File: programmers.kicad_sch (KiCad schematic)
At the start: 9 parts, among them J10 Conn_ARM_JTAG_SWD_10, SW1 KMR231NG LFS, U8 MKL02Z32VFG4

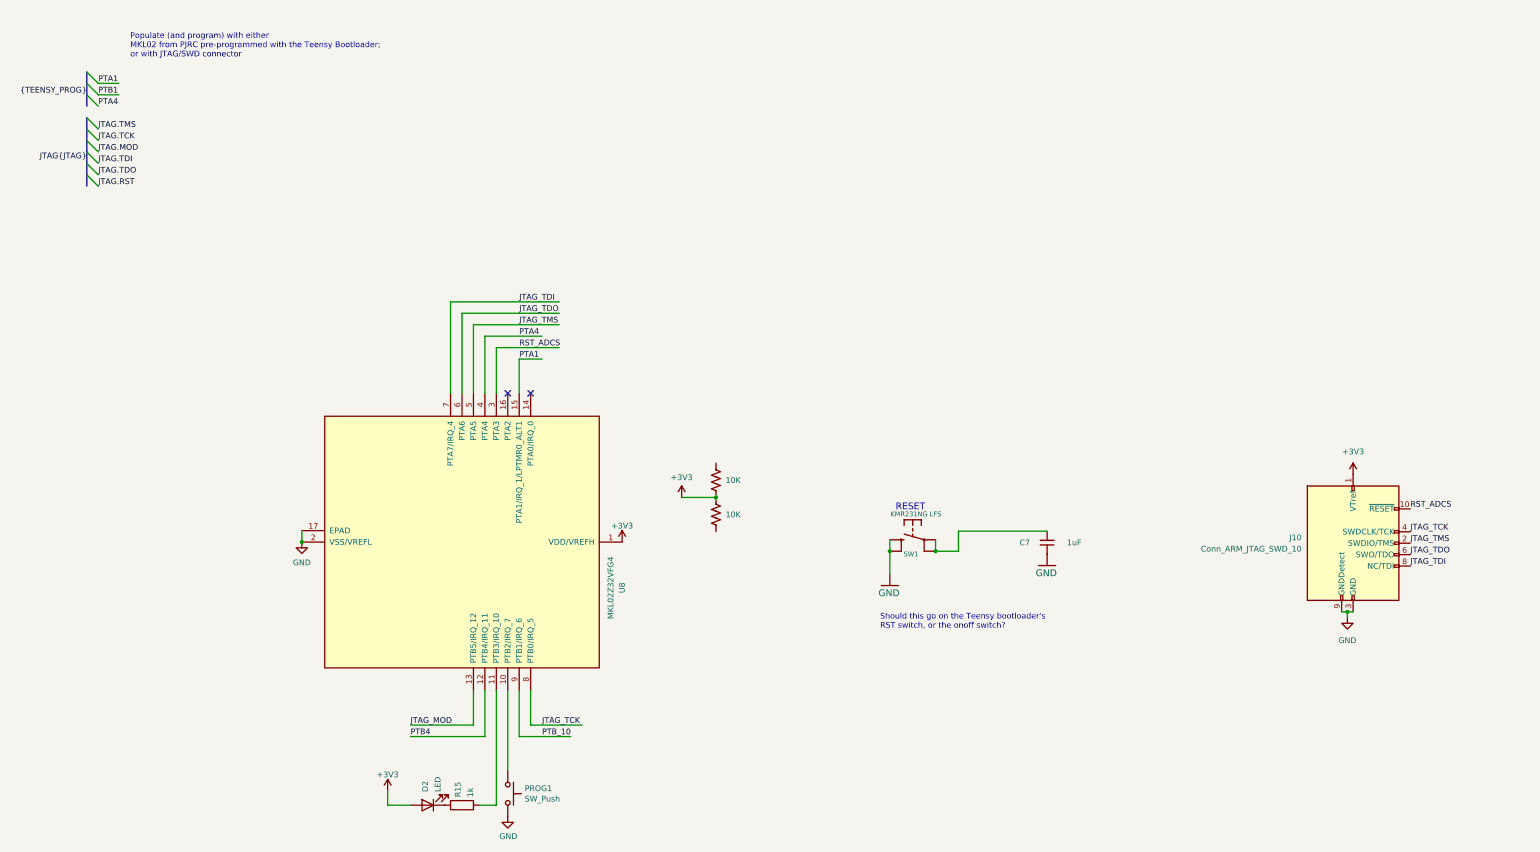
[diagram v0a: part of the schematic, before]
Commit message: schematic update
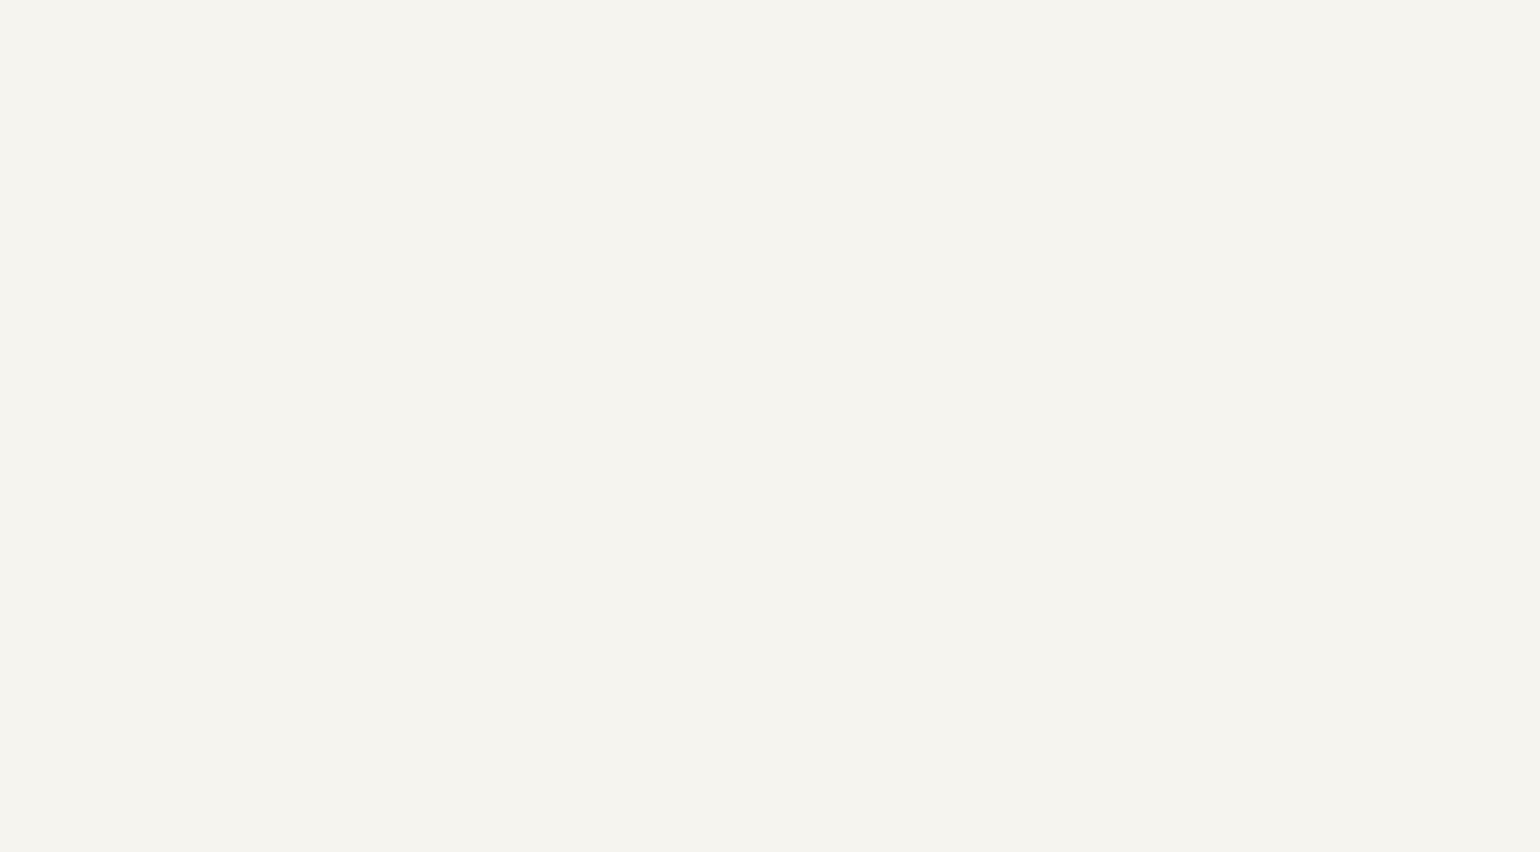
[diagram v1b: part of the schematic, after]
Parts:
- removed C7: 1uF, Capacitor_SMD:C_0603_1608Metric, symbol mainboard:C_Small
- removed D2: LED, LED_SMD:LED_0402_1005Metric, symbol Device:LED
- removed J10: Conn_ARM_JTAG_SWD_10, Connector_PinHeader_1.27mm:PinHeader_2x05_P1.27mm_Vertical_SMD, symbol Connector:Conn_ARM_JTAG_SWD_10
- removed PROG1: SW_Push, ToyTronics:KMR241GLFS, symbol Switch:SW_Push
- removed R15: 1k, Resistor_SMD:R_0402_1005Metric, symbol Device:R
- removed R17, R20: 10K, Resistor_SMD:R_0603_1608Metric, symbol Device:R_US
- removed SW1: KMR231NG LFS, mainboard:BTN_KMR2_4.6X2.8, symbol mainboard:SWITCH_SMT4.6X2.8
- removed U8: MKL02Z32VFG4, Package_DFN_QFN:QFN-16-1EP_3x3mm_P0.5mm_EP1.8x1.8mm, symbol MCU_NXP_Kinetis:MKL02Z32VFG4
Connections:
- no-connect marks 2 -> 0
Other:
- note removed: "Populate (and program) with either MKL02 from PJRC pre-programmed with the Teensy Bootloader; or with JTAG/SWD connector"
- note removed: "RESET"
- note removed: "Should this go on the Teensy bootloader's RST switch, or the onoff switch?"
